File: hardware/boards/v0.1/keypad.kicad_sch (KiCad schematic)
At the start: 78 parts, among them SW1 TRIG1, SW10 TRIG10, SW11 TRIG11, SW12 TRIG12, SW13 TRIG13, SW14 TRIG14, SW15 TRIG15, SW16 TRIG16, SW17 MENU0, SW19 MENU1, SW2 TRIG2, SW20 MENU2, SW21 MENU3, SW3 TRIG3, SW4 TRIG4, SW5 TRIG5, SW6 TRIG6, SW7 TRIG7, SW8 TRIG8, SW9 TRIG9, U25 TCA8418RTWR, U38 ADS7128IRTER

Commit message: feat: various DFM cleanup steps
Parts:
- SW1, SW10, SW11, SW12, SW13, SW14, SW15, SW16, SW2, SW3, SW4, SW5, SW6, SW7, SW8, SW9: JLC (none) -> C5333465
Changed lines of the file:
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@@
 			)
 		)
-		(property "JLC" ""
+		(property "JLC" "C5333465"
 			(at 215.9 157.48 0)
 			(effects
@@
 					(size 1.27 1.27)
 				)
+				(hide yes)
 			)
 		)
@@
 			)
 		)
-		(property "JLC" ""
+		(property "JLC" "C5333465"
 			(at 167.64 142.24 0)
 			(effects
@@
 					(size 1.27 1.27)
 				)
+				(hide yes)
 			)
 		)
@@
 			)
 		)
-		(property "JLC" ""
+		(property "JLC" "C5333465"
 			(at 167.64 50.8 0)
 			(effects
@@
 					(size 1.27 1.27)
 				)
+				(hide yes)
 			)
 		)
@@
 			)
 		)
-		(property "JLC" ""
+		(property "JLC" "C5333465"
 			(at 215.9 142.24 0)
 			(effects
@@
 					(size 1.27 1.27)
 				)
+				(hide yes)
 			)
 		)
@@
 			)
 		)
-		(property "JLC" ""
+		(property "JLC" "C5333465"
 			(at 191.77 142.24 0)
 			(effects
@@
 					(size 1.27 1.27)
 				)
+				(hide yes)
 			)
 		)
@@
 			)
 		)
-		(property "JLC" ""
+		(property "JLC" "C5333465"
 			(at 215.9 127 0)
 			(effects
@@
 					(size 1.27 1.27)
 				)
+				(hide yes)
 			)
 		)
@@
 			)
 		)
-		(property "JLC" ""
+		(property "JLC" "C5333465"
 			(at 143.51 111.76 0)
 			(effects
@@
 					(size 1.27 1.27)
 				)
+				(hide yes)
 			)
 		)
@@
 			)
 		)
-		(property "JLC" ""
+		(property "JLC" "C5333465"
 			(at 142.24 81.28 0)
 			(effects
@@
 					(size 1.27 1.27)
 				)
+				(hide yes)
 			)
 		)
@@
 			)
 		)
-		(property "JLC" ""
+		(property "JLC" "C5333465"
 			(at 193.04 66.04 0)
 			(effects
@@
 					(size 1.27 1.27)
 				)
+				(hide yes)
 			)
 		)
@@
 			)
 		)
-		(property "JLC" ""
+		(property "JLC" "C5333465"
 			(at 191.77 111.76 0)
 			(effects
@@
 					(size 1.27 1.27)
 				)
+				(hide yes)
 			)
 		)
@@
 			)
 		)
-		(property "JLC" ""
+		(property "JLC" "C5333465"
 			(at 218.44 35.56 0)
 			(effects
@@
 					(size 1.27 1.27)
 				)
+				(hide yes)
 			)
 		)
@@
 			)
 		)
-		(property "JLC" ""
+		(property "JLC" "C5333465"
 			(at 193.04 81.28 0)
 			(effects
@@
 					(size 1.27 1.27)
 				)
+				(hide yes)
 			)
 		)
@@
 			)
 		)
-		(property "JLC" ""
+		(property "JLC" "C5333465"
 			(at 218.44 81.28 0)
 			(effects
@@
 					(size 1.27 1.27)
 				)
+				(hide yes)
 			)
 		)
@@
 			)
 		)
-		(property "JLC" ""
+		(property "JLC" "C5333465"
 			(at 142.24 35.56 0)
 			(effects
@@
 					(size 1.27 1.27)
 				)
+				(hide yes)
 			)
 		)
@@
 			)
 		)
-		(property "JLC" ""
+		(property "JLC" "C5333465"
 			(at 167.64 111.76 0)
 			(effects
@@
 					(size 1.27 1.27)
 				)
+				(hide yes)
 			)
 		)
@@
 			)
 		)
-		(property "JLC" ""
+		(property "JLC" "C5333465"
 			(at 218.44 50.8 0)
 			(effects
@@
 					(size 1.27 1.27)
 				)
+				(hide yes)
 			)
 		)
@@
 			)
 		)
-		(property "JLC" ""
+		(property "JLC" "C5333465"
 			(at 218.44 66.04 0)
 			(effects
@@
 					(size 1.27 1.27)
 				)
+				(hide yes)
 			)
 		)
@@
 			)
 		)
-		(property "JLC" ""
+		(property "JLC" "C5333465"
 			(at 215.9 111.76 0)
 			(effects
@@
 					(size 1.27 1.27)
 				)
+				(hide yes)
 			)
 		)
@@
 			)
 		)
-		(property "JLC" ""
+		(property "JLC" "C5333465"
 			(at 167.64 81.28 0)
 			(effects
@@
 					(size 1.27 1.27)
 				)
+				(hide yes)
 			)
 		)
@@
 			)
 		)
-		(property "JLC" ""
+		(property "JLC" "C5333465"
 			(at 142.24 66.04 0)
 			(effects
@@
 					(size 1.27 1.27)
 				)
+				(hide yes)
 			)
 		)
@@
 			)
 		)
-		(property "JLC" ""
+		(property "JLC" "C5333465"
 			(at 143.51 157.48 0)
 			(effects
@@
 					(size 1.27 1.27)
 				)
+				(hide yes)
 			)
 		)
@@
 			)
 		)
-		(property "JLC" ""
+		(property "JLC" "C5333465"
 			(at 142.24 50.8 0)
 			(effects
@@
 					(size 1.27 1.27)
 				)
+				(hide yes)
 			)
 		)
@@
 			)
 		)
-		(property "JLC" ""
+		(property "JLC" "C5333465"
 			(at 167.64 66.04 0)
 			(effects
@@
 					(size 1.27 1.27)
 				)
+				(hide yes)
 			)
 		)
@@
 			)
 		)
-		(property "JLC" ""
+		(property "JLC" "C5333465"
 			(at 143.51 127 0)
 			(effects
@@
 					(size 1.27 1.27)
 				)
+				(hide yes)
 			)
 		)
@@
 			)
 		)
-		(property "JLC" ""
+		(property "JLC" "C5333465"
 			(at 167.64 157.48 0)
 			(effects
@@
 					(size 1.27 1.27)
 				)
+				(hide yes)
 			)
 		)
@@
 			)
 		)
-		(property "JLC" ""
+		(property "JLC" "C5333465"
 			(at 191.77 157.48 0)
 			(effects
@@
 					(size 1.27 1.27)
 				)
+				(hide yes)
 			)
 		)
@@
 			)
 		)
-		(property "JLC" ""
+		(property "JLC" "C5333465"
 			(at 167.64 35.56 0)
 			(effects
@@
 					(size 1.27 1.27)
 				)
+				(hide yes)
 			)
 		)
@@
 			)
 		)
-		(property "JLC" ""
+		(property "JLC" "C5333465"
 			(at 193.04 35.56 0)
 			(effects
@@
 					(size 1.27 1.27)
 				)
+				(hide yes)
 			)
 		)
@@
 			)
 		)
-		(property "JLC" ""
+		(property "JLC" "C5333465"
 			(at 167.64 127 0)
 			(effects
@@
 					(size 1.27 1.27)
 				)
+				(hide yes)
 			)
 		)
@@
 			)
 		)
-		(property "JLC" ""
+		(property "JLC" "C5333465"
 			(at 191.77 127 0)
 			(effects
@@
 					(size 1.27 1.27)
 				)
+				(hide yes)
 			)
 		)
@@
 			)
 		)
-		(property "JLC" ""
+		(property "JLC" "C5333465"
 			(at 143.51 142.24 0)
 			(effects
@@
 					(size 1.27 1.27)
 				)
+				(hide yes)
 			)
 		)
@@
 			)
 		)
-		(property "JLC" ""
+		(property "JLC" "C5333465"
 			(at 193.04 50.8 0)
 			(effects
@@
 					(size 1.27 1.27)
 				)
+				(hide yes)
 			)
 		)

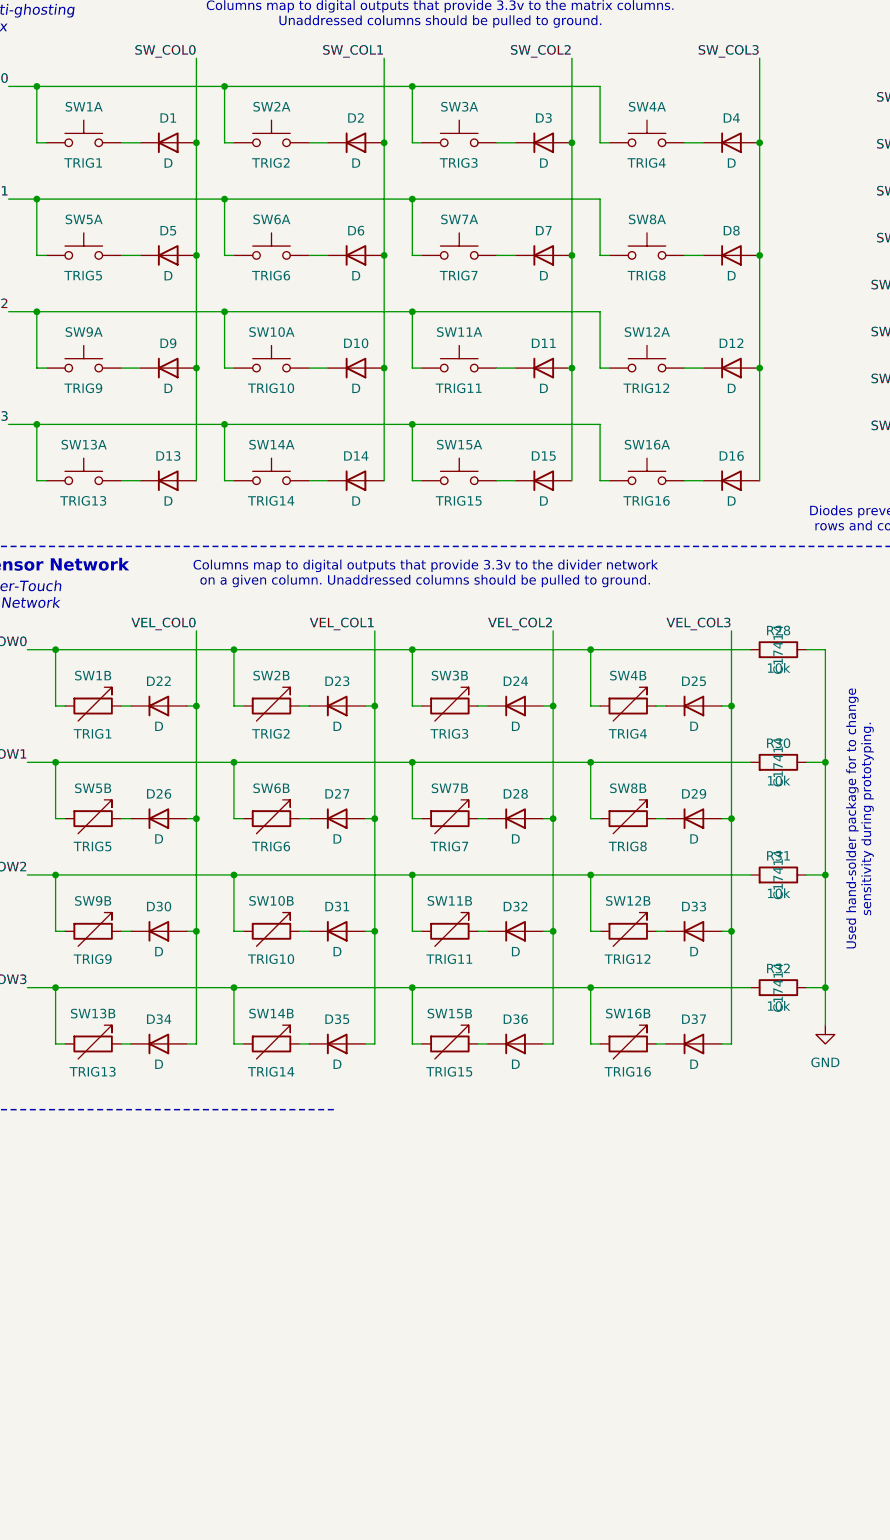
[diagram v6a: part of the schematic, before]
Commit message: feat: set correct footprint for matrix diodes
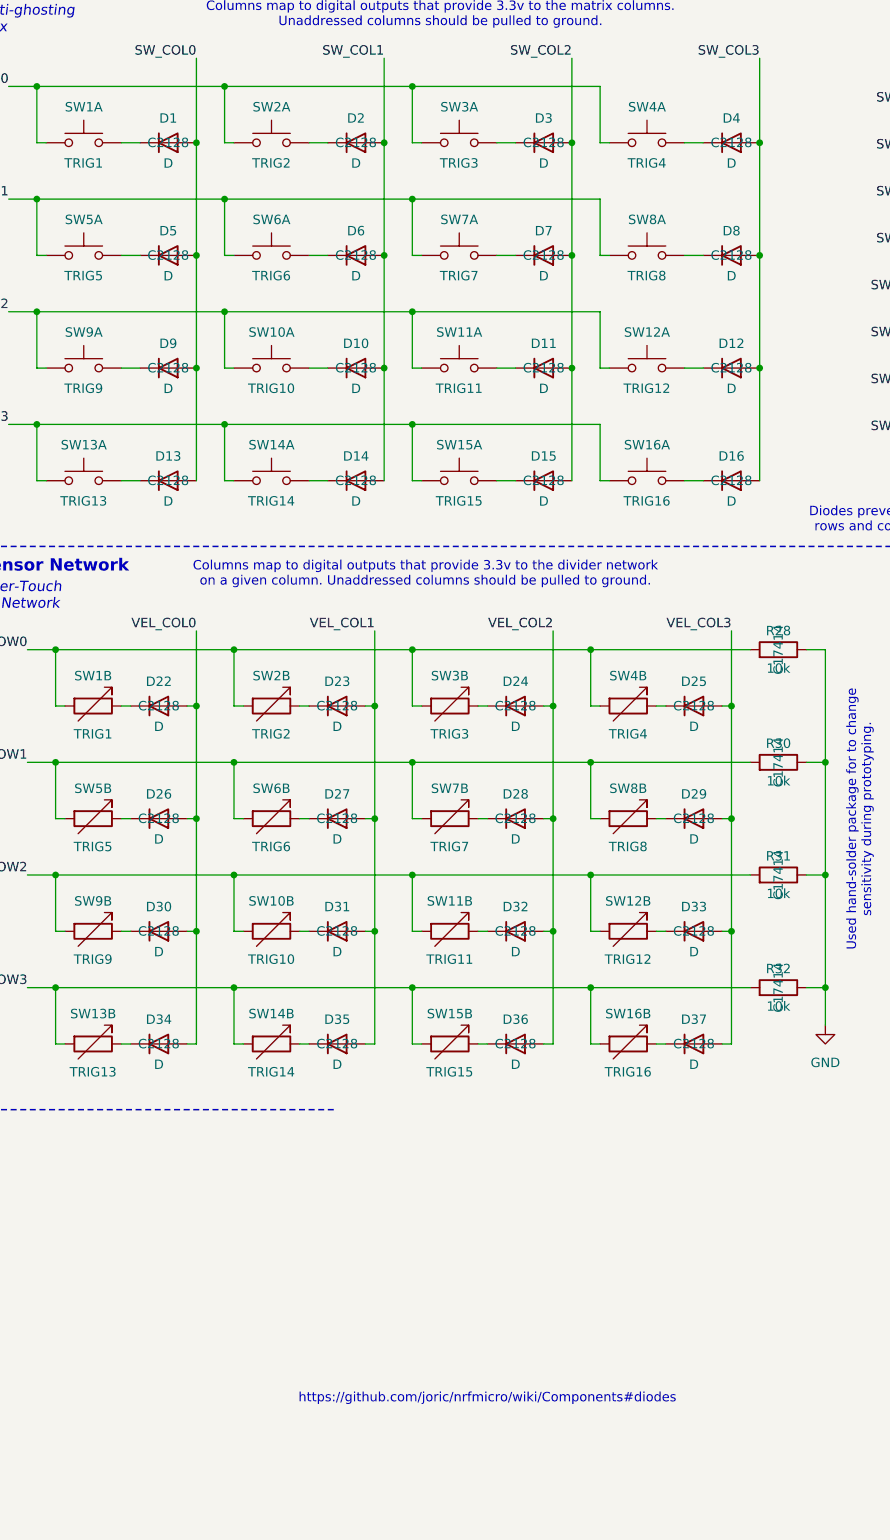
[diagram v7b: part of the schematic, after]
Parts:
- D1, D10, D11, D12, D13, D14, D15, D16, D2, D22, D23, D24, D25, D26, D27, D28, D29, D3, D30, D31, D32, D33, D34, D35, D36, D37, D4, D5, D6, D7, D8, D9: footprint Diode_SMD:D_0402_1005Metric -> Diode_SMD:D_SOD-123; JLC (none) -> C2128
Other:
- note added: "https://github.com/joric/nrfmicro/wiki/Components#diodes"
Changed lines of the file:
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@@
 		)
 	)
+	(text "https://github.com/joric/nrfmicro/wiki/Components#diodes"
+		(exclude_from_sim no)
+		(at 196.85 205.486 0)
+		(effects
+			(font
+				(size 1.27 1.27)
+				(color 132 132 132 1)
+			)
+		)
+	)
 	(text "Keypad Decoder"
 		(exclude_from_sim no)
@@
 			)
 		)
-		(property "Footprint" "Diode_SMD:D_0402_1005Metric"
+		(property "Footprint" "Diode_SMD:D_SOD-123"
 			(at 179.07 35.56 0)
 			(effects
@@
 			)
 		)
-		(property "JLC" ""
+		(property "JLC" "C2128"
 			(at 179.07 35.56 0)
 			(effects
@@
 			)
 		)
-		(property "Footprint" "Diode_SMD:D_0402_1005Metric"
+		(property "Footprint" "Diode_SMD:D_SOD-123"
 			(at 224.79 127 0)
 			(effects
@@
 			)
 		)
-		(property "JLC" ""
+		(property "JLC" "C2128"
 			(at 224.79 127 0)
 			(effects
@@
 			)
 		)
-		(property "Footprint" "Diode_SMD:D_0402_1005Metric"
+		(property "Footprint" "Diode_SMD:D_SOD-123"
 			(at 152.4 127 0)
 			(effects
@@
 			)
 		)
-		(property "JLC" ""
+		(property "JLC" "C2128"
 			(at 152.4 127 0)
 			(effects
@@
 			)
 		)
-		(property "Footprint" "Diode_SMD:D_0402_1005Metric"
+		(property "Footprint" "Diode_SMD:D_SOD-123"
 			(at 204.47 50.8 0)
 			(effects
@@
 			)
 		)
-		(property "JLC" ""
+		(property "JLC" "C2128"
 			(at 204.47 50.8 0)
 			(effects
@@
 			)
 		)
-		(property "Footprint" "Diode_SMD:D_0402_1005Metric"
+		(property "Footprint" "Diode_SMD:D_SOD-123"
 			(at 176.53 111.76 0)
 			(effects
@@
 			)
 		)
-		(property "JLC" ""
+		(property "JLC" "C2128"
 			(at 176.53 111.76 0)
 			(effects
@@
 			)
 		)
-		(property "Footprint" "Diode_SMD:D_0402_1005Metric"
+		(property "Footprint" "Diode_SMD:D_SOD-123"
 			(at 229.87 66.04 0)
 			(effects
@@
 			)
 		)
-		(property "JLC" ""
+		(property "JLC" "C2128"
 			(at 229.87 66.04 0)
 			(effects
@@
 			)
 		)
-		(property "Footprint" "Diode_SMD:D_0402_1005Metric"
+		(property "Footprint" "Diode_SMD:D_SOD-123"
 			(at 153.67 35.56 0)
 			(effects
@@
 			)
 		)
-		(property "JLC" ""
+		(property "JLC" "C2128"
 			(at 153.67 35.56 0)
 			(effects
@@
 			)
 		)
-		(property "Footprint" "Diode_SMD:D_0402_1005Metric"
+		(property "Footprint" "Diode_SMD:D_SOD-123"
 			(at 200.66 142.24 0)
 			(effects
@@
 			)
 		)
-		(property "JLC" ""
+		(property "JLC" "C2128"
 			(at 200.66 142.24 0)
 			(effects
@@
 			)
 		)
-		(property "Footprint" "Diode_SMD:D_0402_1005Metric"
+		(property "Footprint" "Diode_SMD:D_SOD-123"
 			(at 200.66 111.76 0)
 			(effects
@@
 			)
 		)
-		(property "JLC" ""
+		(property "JLC" "C2128"
 			(at 200.66 111.76 0)
 			(effects
@@
 			)
 		)
-		(property "Footprint" "Diode_SMD:D_0402_1005Metric"
+		(property "Footprint" "Diode_SMD:D_SOD-123"
 			(at 179.07 50.8 0)
 			(effects
@@
 			)
 		)
-		(property "JLC" ""
+		(property "JLC" "C2128"
 			(at 179.07 50.8 0)
 			(effects
@@
 			)
 		)
-		(property "Footprint" "Diode_SMD:D_0402_1005Metric"
+		(property "Footprint" "Diode_SMD:D_SOD-123"
 			(at 179.07 81.28 0)
 			(effects
@@
 			)
 		)
-		(property "JLC" ""
+		(property "JLC" "C2128"
 			(at 179.07 81.28 0)
 			(effects
@@
 			)
 		)
-		(property "Footprint" "Diode_SMD:D_0402_1005Metric"
+		(property "Footprint" "Diode_SMD:D_SOD-123"
 			(at 153.67 81.28 0)
 			(effects
@@
 			)
 		)
-		(property "JLC" ""
+		(property "JLC" "C2128"
 			(at 153.67 81.28 0)
 			(effects
@@
 			)
 		)
-		(property "Footprint" "Diode_SMD:D_0402_1005Metric"
+		(property "Footprint" "Diode_SMD:D_SOD-123"
 			(at 224.79 157.48 0)
 			(effects
@@
 			)
 		)
-		(property "JLC" ""
+		(property "JLC" "C2128"
 			(at 224.79 157.48 0)
 			(effects
@@
 			)
 		)
-		(property "Footprint" "Diode_SMD:D_0402_1005Metric"
+		(property "Footprint" "Diode_SMD:D_SOD-123"
 			(at 224.79 142.24 0)
 			(effects
@@
 			)
 		)
-		(property "JLC" ""
+		(property "JLC" "C2128"
 			(at 224.79 142.24 0)
 			(effects
@@
 			)
 		)
-		(property "Footprint" "Diode_SMD:D_0402_1005Metric"
+		(property "Footprint" "Diode_SMD:D_SOD-123"
 			(at 152.4 142.24 0)
 			(effects
@@
 			)
 		)
-		(property "JLC" ""
+		(property "JLC" "C2128"
 			(at 152.4 142.24 0)
 			(effects
@@
 			)
 		)
-		(property "Footprint" "Diode_SMD:D_0402_1005Metric"
+		(property "Footprint" "Diode_SMD:D_SOD-123"
 			(at 204.47 35.56 0)
 			(effects
@@
 			)
 		)
-		(property "JLC" ""
+		(property "JLC" "C2128"
 			(at 204.47 35.56 0)
 			(effects
@@
 			)
 		)
-		(property "Footprint" "Diode_SMD:D_0402_1005Metric"
+		(property "Footprint" "Diode_SMD:D_SOD-123"
 			(at 152.4 111.76 0)
 			(effects
@@
 			)
 		)
-		(property "JLC" ""
+		(property "JLC" "C2128"
 			(at 152.4 111.76 0)
 			(effects
@@
 			)
 		)
-		(property "Footprint" "Diode_SMD:D_0402_1005Metric"
+		(property "Footprint" "Diode_SMD:D_SOD-123"
 			(at 152.4 157.48 0)
 			(effects
@@
 			)
 		)
-		(property "JLC" ""
+		(property "JLC" "C2128"
 			(at 152.4 157.48 0)
 			(effects
@@
 			)
 		)
-		(property "Footprint" "Diode_SMD:D_0402_1005Metric"
+		(property "Footprint" "Diode_SMD:D_SOD-123"
 			(at 204.47 66.04 0)
 			(effects
@@
 			)
 		)
-		(property "JLC" ""
+		(property "JLC" "C2128"
 			(at 204.47 66.04 0)
 			(effects
@@
 			)
 		)
-		(property "Footprint" "Diode_SMD:D_0402_1005Metric"
+		(property "Footprint" "Diode_SMD:D_SOD-123"
 			(at 204.47 81.28 0)
 			(effects
@@
 			)
 		)
-		(property "JLC" ""
+		(property "JLC" "C2128"
 			(at 204.47 81.28 0)
 			(effects
@@
 			)
 		)
-		(property "Footprint" "Diode_SMD:D_0402_1005Metric"
+		(property "Footprint" "Diode_SMD:D_SOD-123"
 			(at 200.66 127 0)
 			(effects
@@
 			)
 		)
-		(property "JLC" ""
+		(property "JLC" "C2128"
 			(at 200.66 127 0)
 			(effects
@@
 			)
 		)
-		(property "Footprint" "Diode_SMD:D_0402_1005Metric"
+		(property "Footprint" "Diode_SMD:D_SOD-123"
 			(at 229.87 50.8 0)
 			(effects
@@
 			)
 		)
-		(property "JLC" ""
+		(property "JLC" "C2128"
 			(at 229.87 50.8 0)
 			(effects
@@
 			)
 		)
-		(property "Footprint" "Diode_SMD:D_0402_1005Metric"
+		(property "Footprint" "Diode_SMD:D_SOD-123"
 			(at 229.87 35.56 0)
 			(effects
@@
 			)
 		)
-		(property "JLC" ""
+		(property "JLC" "C2128"
 			(at 229.87 35.56 0)
 			(effects
@@
 			)
 		)
-		(property "Footprint" "Diode_SMD:D_0402_1005Metric"
+		(property "Footprint" "Diode_SMD:D_SOD-123"
 			(at 224.79 111.76 0)
 			(effects
@@
 			)
 		)
-		(property "JLC" ""
+		(property "JLC" "C2128"
 			(at 224.79 111.76 0)
 			(effects
@@
 			)
 		)
-		(property "Footprint" "Diode_SMD:D_0402_1005Metric"
+		(property "Footprint" "Diode_SMD:D_SOD-123"
 			(at 153.67 50.8 0)
 			(effects
@@
 			)
 		)
-		(property "JLC" ""
+		(property "JLC" "C2128"
 			(at 153.67 50.8 0)
 			(effects
@@
 			)
 		)
-		(property "Footprint" "Diode_SMD:D_0402_1005Metric"
+		(property "Footprint" "Diode_SMD:D_SOD-123"
 			(at 153.67 66.04 0)
 			(effects
@@
 			)
 		)
-		(property "JLC" ""
+		(property "JLC" "C2128"
 			(at 153.67 66.04 0)
 			(effects
@@
 			)
 		)
-		(property "Footprint" "Diode_SMD:D_0402_1005Metric"
+		(property "Footprint" "Diode_SMD:D_SOD-123"
 			(at 176.53 157.48 0)
 			(effects
@@
 			)
 		)
-		(property "JLC" ""
+		(property "JLC" "C2128"
 			(at 176.53 157.48 0)
 			(effects
@@
 			)
 		)
-		(property "Footprint" "Diode_SMD:D_0402_1005Metric"
+		(property "Footprint" "Diode_SMD:D_SOD-123"
 			(at 229.87 81.28 0)
 			(effects
@@
 			)
 		)
-		(property "JLC" ""
+		(property "JLC" "C2128"
 			(at 229.87 81.28 0)
 			(effects
@@
 			)
 		)
-		(property "Footprint" "Diode_SMD:D_0402_1005Metric"
+		(property "Footprint" "Diode_SMD:D_SOD-123"
 			(at 200.66 157.48 0)
 			(effects
@@
 			)
 		)
-		(property "JLC" ""
+		(property "JLC" "C2128"
 			(at 200.66 157.48 0)
 			(effects
@@
 			)
 		)
-		(property "Footprint" "Diode_SMD:D_0402_1005Metric"
+		(property "Footprint" "Diode_SMD:D_SOD-123"
 			(at 176.53 127 0)
 			(effects
@@
 			)
 		)
-		(property "JLC" ""
+		(property "JLC" "C2128"
 			(at 176.53 127 0)
 			(effects
@@
 			)
 		)
-		(property "Footprint" "Diode_SMD:D_0402_1005Metric"
+		(property "Footprint" "Diode_SMD:D_SOD-123"
 			(at 176.53 142.24 0)
 			(effects
@@
 			)
 		)
-		(property "JLC" ""
+		(property "JLC" "C2128"
 			(at 176.53 142.24 0)
 			(effects
@@
 			)
 		)
-		(property "Footprint" "Diode_SMD:D_0402_1005Metric"
+		(property "Footprint" "Diode_SMD:D_SOD-123"
 			(at 179.07 66.04 0)
 			(effects
@@
 			)
 		)
-		(property "JLC" ""
+		(property "JLC" "C2128"
 			(at 179.07 66.04 0)
 			(effects

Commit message: feat: more BOM selection
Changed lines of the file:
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@@
 					(size 1.27 1.27)
 				)
+				(hide yes)
 			)
 		)
@@
 					(size 1.27 1.27)
 				)
+				(hide yes)
 			)
 		)
@@
 					(size 1.27 1.27)
 				)
+				(hide yes)
 			)
 		)
@@
 					(size 1.27 1.27)
 				)
+				(hide yes)
 			)
 		)
@@
 					(size 1.27 1.27)
 				)
+				(hide yes)
 			)
 		)
@@
 					(size 1.27 1.27)
 				)
+				(hide yes)
 			)
 		)
@@
 					(size 1.27 1.27)
 				)
+				(hide yes)
 			)
 		)
@@
 					(size 1.27 1.27)
 				)
+				(hide yes)
 			)
 		)
@@
 					(size 1.27 1.27)
 				)
+				(hide yes)
 			)
 		)
@@
 					(size 1.27 1.27)
 				)
+				(hide yes)
 			)
 		)
@@
 					(size 1.27 1.27)
 				)
+				(hide yes)
 			)
 		)
@@
 					(size 1.27 1.27)
 				)
+				(hide yes)
 			)
 		)
@@
 					(size 1.27 1.27)
 				)
+				(hide yes)
 			)
 		)
@@
 					(size 1.27 1.27)
 				)
+				(hide yes)
 			)
 		)
@@
 					(size 1.27 1.27)
 				)
+				(hide yes)
 			)
 		)
@@
 					(size 1.27 1.27)
 				)
+				(hide yes)
 			)
 		)
@@
 					(size 1.27 1.27)
 				)
+				(hide yes)
 			)
 		)
@@
 					(size 1.27 1.27)
 				)
+				(hide yes)
 			)
 		)
@@
 					(size 1.27 1.27)
 				)
+				(hide yes)
 			)
 		)
@@
 					(size 1.27 1.27)
 				)
+				(hide yes)
 			)
 		)
@@
 					(size 1.27 1.27)
 				)
+				(hide yes)
 			)
 		)
@@
 					(size 1.27 1.27)
 				)
+				(hide yes)
 			)
 		)
@@
 					(size 1.27 1.27)
 				)
+				(hide yes)
 			)
 		)
@@
 					(size 1.27 1.27)
 				)
+				(hide yes)
 			)
 		)
@@
 					(size 1.27 1.27)
 				)
+				(hide yes)
 			)
 		)
@@
 					(size 1.27 1.27)
 				)
+				(hide yes)
 			)
 		)
@@
 					(size 1.27 1.27)
 				)
+				(hide yes)
 			)
 		)
@@
 					(size 1.27 1.27)
 				)
+				(hide yes)
 			)
 		)
@@
 					(size 1.27 1.27)
 				)
+				(hide yes)
 			)
 		)
@@
 					(size 1.27 1.27)
 				)
+				(hide yes)
 			)
 		)
@@
 					(size 1.27 1.27)
 				)
+				(hide yes)
 			)
 		)
@@
 					(size 1.27 1.27)
 				)
+				(hide yes)
 			)
 		)
